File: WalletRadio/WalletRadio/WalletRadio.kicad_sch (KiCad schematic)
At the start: 32 parts, among them Q1 BSP315P, Q1002 Q_NPN_ECB, SW1001 SW_DIP_x01, U1 LM324A, U2 BB201

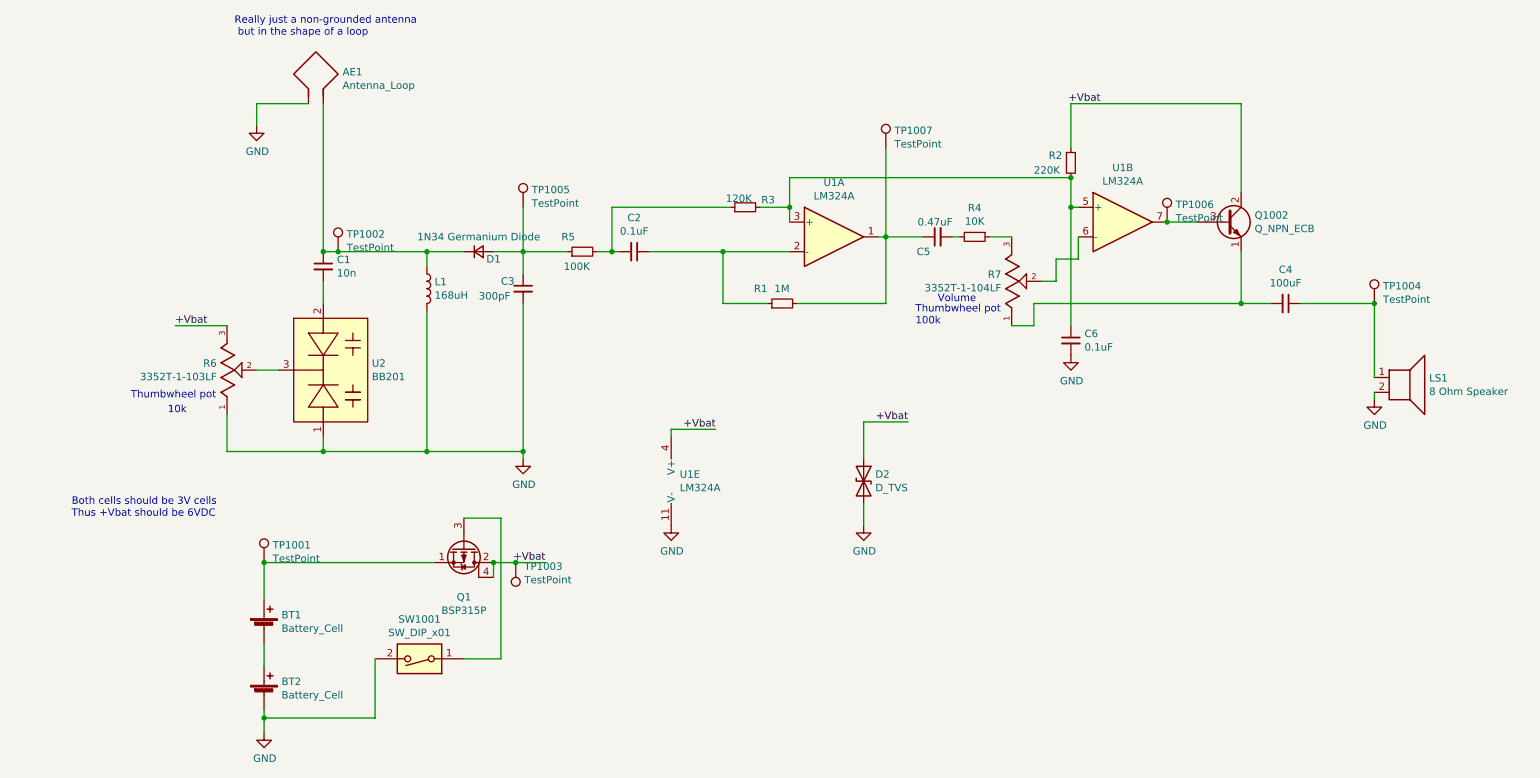
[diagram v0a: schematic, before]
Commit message: Working on PCB antenna
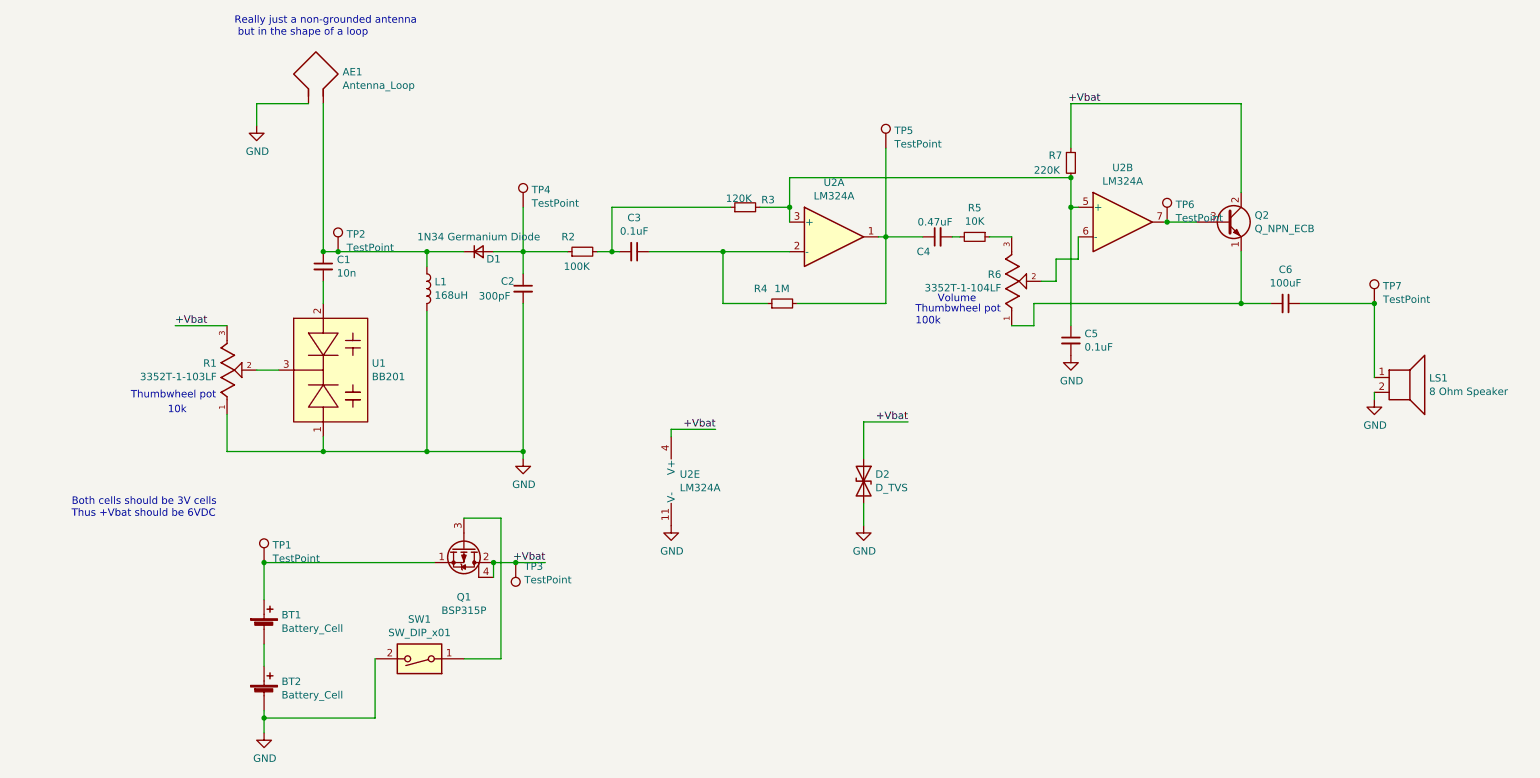
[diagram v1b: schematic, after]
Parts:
- renumbered C3 to C2, C2 to C3, C5 to C4, C6 to C5, C4 to C6, Q1002 to Q2, R6 to R1, R5 to R2, R1 to R4, R4 to R5, R7 to R6, R2 to R7, SW1001 to SW1, TP1001 to TP1, TP1002 to TP2, TP1003 to TP3, TP1005 to TP4, TP1007 to TP5, TP1006 to TP6, TP1004 to TP7, U2 to U1, U1 to U2

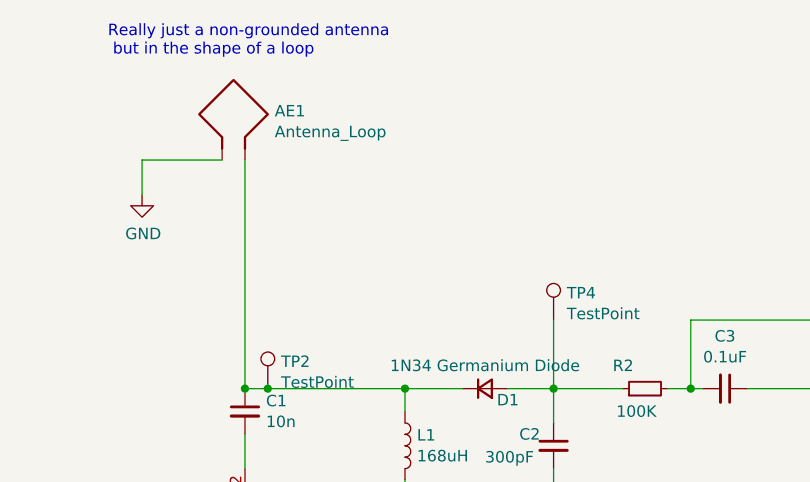
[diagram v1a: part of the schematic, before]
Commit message: More embedded antenna work
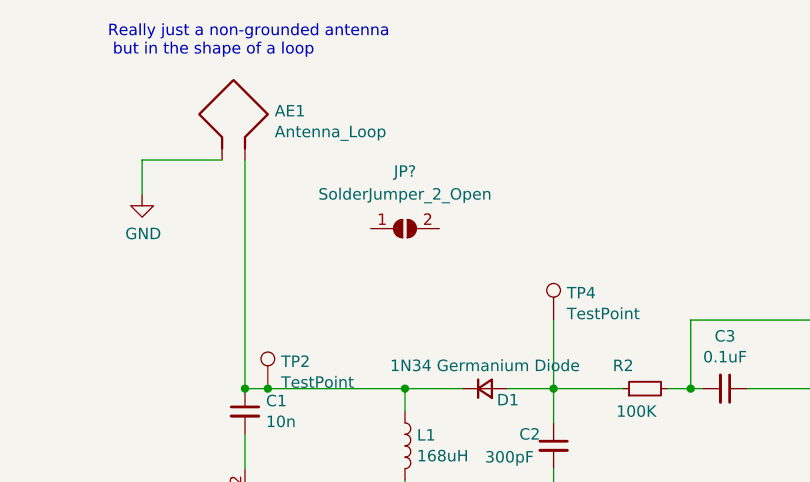
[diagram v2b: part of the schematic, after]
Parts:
- added JP?: SolderJumper_2_Open, symbol Jumper:SolderJumper_2_Open
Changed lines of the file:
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@@
     (pin "3")
+  )
+  (symbol (lib_id "Jumper:SolderJumper_2_Open") (at 90.17 55.88 0) (unit 1)
+    (in_bom yes) (on_board yes) (fields_autoplaced)
+    (property "Reference" "JP?" (id 0) (at 90.17 49.53 0))
+    (property "Value" "SolderJumper_2_Open" (id 1) (at 90.17 52.07 0))
+    (property "Footprint" "" (id 2) (at 90.17 55.88 0)
+      (effects (font (size 1.27 1.27)) hide)
+    )
+    (property "Datasheet" "~" (id 3) (at 90.17 55.88 0)
+      (effects (font (size 1.27 1.27)) hide)
+    )
+    (pin "1")
+    (pin "2")
   )
   (sheet_instances
@@
       (reference "D2") (unit 1) (value "D_TVS") (footprint "WalletRadio:5.0SMDJ9.0CA")
     )
+    (path "/d3af3a67-42ec-49ee-ba99-a58410822424"
+      (reference "JP?") (unit 1) (value "SolderJumper_2_Open") (footprint "")
+    )
     (path "/00000000-0000-0000-0000-00005ef68f6a"

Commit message: Slight edits to PCB
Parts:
- removed JP?: SolderJumper_2_Open, symbol Jumper:SolderJumper_2_Open
- added U2: BB201, Package_TO_SOT_SMD:SOT-23_Handsoldering, symbol WalletRadioLib:BB201
- renumbered U2 to U3
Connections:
- net GND: now also U2.1
- net at C1.2, U1.2: now also U2.2
- net at R1.2, U1.3: now also U2.3
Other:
- moved on the sheet: R1, U1

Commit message: Edited power switch, cleaned up layout
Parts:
- removed SW1: SW_DIP_x01, WalletRadio:CUS-12TB_Switch, symbol Switch:SW_DIP_x01
- added SW1: SW_SPDT, WalletRadio:CUS-12TB_Switch, symbol Switch:SW_SPDT
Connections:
- net GND: now also SW1.1 (A)
- net at Q1.3 (G): now also SW1.2 (B)
- net at BT1.1 (+), Q1.1 (S), TP1.1: now also SW1.3 (C)
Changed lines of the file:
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@@
   (junction (at 217.17 68.58) (diameter 0) (color 0 0 0 0)
   )
+  (junction (at 81.28 127) (diameter 0) (color 0 0 0 0)
+  )
   (junction (at 168.91 71.12) (diameter 0) (color 0 0 0 0)
   )
@@
     (stroke (width 0) (type default) (color 0 0 0 0))
   )
-  (wire (pts (xy 81.28 153.67) (xy 81.28 143.51))
+  (wire (pts (xy 81.28 153.67) (xy 81.28 146.05))
     (stroke (width 0) (type default) (color 0 0 0 0))
   )
@@
     (stroke (width 0) (type default) (color 0 0 0 0))
   )
+  (wire (pts (xy 86.36 140.97) (xy 81.28 140.97))
+    (stroke (width 0) (type default) (color 0 0 0 0))
+  )
   (wire (pts (xy 198.12 78.74) (xy 195.58 78.74))
     (stroke (width 0) (type default) (color 0 0 0 0))
@@
     (stroke (width 0) (type default) (color 0 0 0 0))
   )
+  (wire (pts (xy 81.28 140.97) (xy 81.28 127))
+    (stroke (width 0) (type default) (color 0 0 0 0))
+  )
   (wire (pts (xy 140.97 82.55) (xy 140.97 73.66))
     (stroke (width 0) (type default) (color 0 0 0 0))
@@
     (stroke (width 0) (type default) (color 0 0 0 0))
   )
+  (wire (pts (xy 81.28 146.05) (xy 86.36 146.05))
+    (stroke (width 0) (type default) (color 0 0 0 0))
+  )
   (wire (pts (xy 69.85 48.26) (xy 60.96 48.26))
     (stroke (width 0) (type default) (color 0 0 0 0))
@@
     (stroke (width 0) (type default) (color 0 0 0 0))
   )
-  (wire (pts (xy 62.23 127) (xy 91.44 127))
+  (wire (pts (xy 62.23 127) (xy 81.28 127))
     (stroke (width 0) (type default) (color 0 0 0 0))
   )
@@
     (stroke (width 0) (type default) (color 0 0 0 0))
   )
+  (wire (pts (xy 81.28 127) (xy 91.44 127))
+    (stroke (width 0) (type default) (color 0 0 0 0))
+  )
   (wire (pts (xy 54.61 105.41) (xy 54.61 107.95))
     (stroke (width 0) (type default) (color 0 0 0 0))
@@
   )
   (text "Both cells should be 3V cells\nThus +Vbat should be 6VDC"
-    (at 29.21 119.38 0)
+    (at 29.21 133.35 0)
     (effects (font (size 1.27 1.27)) (justify left bottom))
   )
@@
     (pin "4")
   )
-  (symbol (lib_id "Switch:SW_DIP_x01") (at 88.9 143.51 180) (unit 1)
-    (in_bom yes) (on_board yes)
-    (property "Reference" "SW1" (id 0) (at 88.9 136.7282 0))
-    (property "Value" "SW_DIP_x01" (id 1) (at 88.9 139.0396 0))
-    (property "Footprint" "WalletRadio:CUS-12TB_Switch" (id 2) (at 88.9 143.51 0)
-      (effects (font (size 1.27 1.27)) hide)
-    )
-    (property "Datasheet" "https://www.digikey.com/product-detail/en/nidec-copal-electronics/CUS-12TB/563-1102-1-ND/1124231" (id 3) (at 88.9 143.51 0)
-      (effects (font (size 1.27 1.27)) hide)
-    )
-    (pin "1")
-    (pin "2")
-  )
   (symbol (lib_id "Amplifier_Operational:LM324A") (at 209.55 68.58 0) (unit 2)
     (in_bom yes) (on_board yes)
@@
     (pin "3")
   )
+  (symbol (lib_id "Switch:SW_SPDT") (at 91.44 143.51 180) (unit 1)
+    (in_bom yes) (on_board yes) (fields_autoplaced)
+    (property "Reference" "SW1" (id 0) (at 91.44 151.13 0))
+    (property "Value" "SW_SPDT" (id 1) (at 91.44 148.59 0))
+    (property "Footprint" "WalletRadio:CUS-12TB_Switch" (id 2) (at 91.44 143.51 0)
+      (effects (font (size 1.27 1.27)) hide)
+    )
+    (property "Datasheet" "https://www.nidec-copal-electronics.com/e/catalog/switch/cus.pdf" (id 3) (at 91.44 143.51 0)
+      (effects (font (size 1.27 1.27)) hide)
+    )
+    (pin "1")
+    (pin "2")
+    (pin "3")
+  )
   (symbol (lib_id "WalletRadioLib:BB201") (at 77.47 93.98 0) (unit 1)
     (in_bom yes) (on_board yes)
@@
       (reference "R7") (unit 1) (value "220K") (footprint "Resistor_SMD:R_0603_1608Metric_Pad1.05x0.95mm_HandSolder")
     )
-    (path "/00000000-0000-0000-0000-00005ef7c51e"
-      (reference "SW1") (unit 1) (value "SW_DIP_x01") (footprint "WalletRadio:CUS-12TB_Switch")
+    (path "/15aca8ef-073f-47a4-a7c9-159fba6de3fc"
+      (reference "SW1") (unit 1) (value "SW_SPDT") (footprint "WalletRadio:CUS-12TB_Switch")
     )
     (path "/00000000-0000-0000-0000-00005efd1cdf"
